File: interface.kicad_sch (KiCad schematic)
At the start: 25 parts, among them J1 QTH-060-03-L-D-A, J2 WE_68715014522_ONE-SIDE, J3 WE_68715014022

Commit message: [#60956] WiP Update symbols references
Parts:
- C1, C2, C3, C4: footprint antmicro-jetson-agx-csi-adapter-footprints:0603-cap -> antmicro-footprints:C_0603_1608Metric; symbol antmicro-jetson-agx-csi-adapter:C_1u_0603 -> antmicroCapacitors0603:C_1u_0603; Author (none) -> Antmicro; License (none) -> Apache-2.0; Manufacturer WALSIN -> KYOCERA AVX; Public (none) -> False
- D1, D2, D3, D4: value LTST-C190GKT -> LED_G_0603_LTST-C190GKT; footprint antmicro-jetson-agx-csi-adapter-footprints:LED_0603 -> antmicro-footprints:LED_0603_1608Metric_G; symbol antmicro-jetson-agx-csi-adapter:LTST-C190GKT -> antmicroLEDIndicationDiscrete:LED_G_0603_LTST-C190GKT; Author (none) -> Antmicro; Color (none) -> Green; License (none) -> Apache-2.0; Manufacturer Lite-On Inc. -> Lite-On; Public (none) -> False
- F1, F2, F3, F4: footprint antmicro-jetson-agx-csi-adapter-footprints:0603-Fuse-Littelfuse-0467 -> antmicro-footprints:F_0603_1608Metric; symbol antmicro-jetson-agx-csi-adapter:04671.25NR -> antmicroFuses:F_1.25A_0603
- J1: value QTH-060-03-L-D-A -> Plug_Samtec_QTH_2x60_QTH-060-03-L-D-A; footprint antmicro-jetson-agx-csi-adapter-footprints:SAMTEC_QTH-060-03-X-D-A -> antmicro-footprints:Conn_Plug_Samtec_QTH_2x60_QTH-060-03-L-D-A; symbol antmicro-jetson-agx-csi-adapter:QTH-060-03-L-D-A -> antmicroB2BConnectors:Plug_Samtec_QTH_2x60_QTH-060-03-L-D-A; Author (none) -> Antmicro; License (none) -> Apache-2.0; Pitch (none) -> 0.5 mm
- R1, R2: footprint antmicro-jetson-agx-csi-adapter-footprints:0805-res -> antmicro-footprints:R_0805_2012Metric; symbol antmicro-jetson-agx-csi-adapter:R_0R_0805 -> antmicroResistorsmisc:R_0R_0805; Author (none) -> Antmicro; Current (none) -> 2.5A; License (none) -> Apache-2.0; Manufacturer VISHAY -> Vishay; Public (none) -> False
- R3, R5: footprint antmicro-jetson-agx-csi-adapter-footprints:0402-res -> antmicro-footprints:R_0402_1005Metric; symbol antmicro-jetson-agx-csi-adapter:R_200R_0402 -> antmicroResistors0402:R_200R_0402
- R4, R6: footprint antmicro-jetson-agx-csi-adapter-footprints:0402-res -> antmicro-footprints:R_0402_1005Metric; symbol antmicro-jetson-agx-csi-adapter:R_470R_0402 -> antmicroResistors0402:R_470R_0402
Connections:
- net GND: now also D1.1 (C), D2.1 (C), D3.1 (C), D4.1 (C), J1.MP; no longer D1.2, D2.2, D3.2, D4.2, J1.G1, J1.G2, J1.G3, J1.G4, J1.G5, J1.G6, J1.G7, J1.G8
- net at R3.2: now also D1.2 (A); no longer D1.1
- net at R4.2: now also D2.2 (A); no longer D2.1
- net at R6.2: now also D4.2 (A); no longer D4.1
- net at R5.2: now also D3.2 (A); no longer D3.1
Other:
- moved on the sheet: C1, C2, C3, C4, R1, R2, TP10, TP11, TP7, TP9

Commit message: [#60956] WiP Update symbols references
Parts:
- removed J2: WE_68715014522_ONE-SIDE, antmicro-jetson-agx-csi-adapter-footprints:WE_68715014522_ONE-SIDE, symbol antmicro-jetson-agx-csi-adapter:WE_68715014522_ONE-SIDE
- removed J3: WE_68715014022, antmicro-jetson-agx-csi-adapter-footprints:WE_68715014022, symbol antmicro-jetson-agx-csi-adapter:WE_68715014022
- added J2: Conn_FFC_WE_68715014522, antmicro-footprints:Conn_FFC_WE_68715014x22, symbol antmicroFCCConnectors:Conn_FFC_WE_68715014522
- added J3: Conn_FFC_WE_68715014022_CUSTOM_FLIPPED, antmicro-footprints:Conn_FFC_WE_68715014x22_CUSTOM_FLIPPED, symbol antmicroFCCConnectors:Conn_FFC_WE_68715014022_CUSTOM_FLIPPED
- F1, F2, F3, F4: value 04671.25NR -> F_1.25A_0603; Author (none) -> Antmicro; License (none) -> Apache-2.0; Manufacturer Littelfuse Inc. -> Littelfuse
- R3, R5: Author (none) -> Antmicro; License (none) -> Apache-2.0; MPN RC0402FR-07200RL -> CR0402-FX-2000GLF; Manufacturer YAGEO -> Bourns; Public (none) -> False; Tolerance (none) -> 1%
- R4, R6: Author (none) -> Antmicro; License (none) -> Apache-2.0; MPN CRCW0402470RFKED -> CR0402-FX-4700GLF; Manufacturer VISHAY -> Bourns; Public (none) -> False; Tolerance (none) -> 1%
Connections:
- net 3V3_FFC_B: now also J2.47, J2.48
- net 3V3_FFC_S: now also J3.47, J3.48
- net 5V_FFC_B: now also J2.49, J2.50
- net 5V_FFC_S: now also J3.49, J3.50
- net CAM0_SCL: now also J2.40
- net CAM0_SDA: now also J2.39
- net CAM1_RST_3V3: now also J3.33
- net CAM1_SCL: now also J2.42
- net CAM1_SDA: now also J2.41
- net CAM2_SCL: now also J3.42
- net CAM2_SDA: now also J3.41
- net CAM3_SCL: now also J3.40
- net CAM3_SDA: now also J3.39
- net CAM_RST_3V3: now also J2.33
- net CSI0_CLK_N: now also J3.28
- net CSI0_CLK_P: now also J3.29
- net CSI0_D0_N: now also J3.25
- net CSI0_D0_P: now also J3.26
- net CSI0_D1_N: now also J3.23
- net CSI0_D1_P: now also J3.24
- net CSI1_D0_N: now also J3.21
- net CSI1_D0_P: now also J3.22
- net CSI1_D1_N: now also J3.19
- net CSI1_D1_P: now also J3.20
- net CSI2_CLK_N: now also J3.10
- net CSI2_CLK_P: now also J3.11
- net CSI2_D0_N: now also J3.7
- net CSI2_D0_P: now also J3.8
- net CSI2_D1_N: now also J3.5
- net CSI2_D1_P: now also J3.6
- net CSI3_D0_N: now also J3.3
- net CSI3_D0_P: now also J3.4
- net CSI3_D1_N: now also J3.1
- net CSI3_D1_P: now also J3.2
- net CSI4_CLK_N: now also J2.29
- net CSI4_CLK_P: now also J2.28
- net CSI4_D0_N: now also J2.25
- net CSI4_D0_P: now also J2.26
- net CSI4_D1_N: now also J2.23
- net CSI4_D1_P: now also J2.24
- net CSI5_D1_N: now also J2.19
- net CSI5_D1_P: now also J2.20
- net CSI6_CLK_N: now also J2.10
- net CSI6_CLK_P: now also J2.11
- net CSI6_D0_N: now also J2.7
- net CSI6_D0_P: now also J2.8
- net CSI6_D1_N: now also J2.5
- net CSI6_D1_P: now also J2.6
- net CSI7_D0_N: now also J2.3
- net CSI7_D0_P: now also J2.4
- net CSI7_D1_N: now also J2.1
- net CSI7_D1_P: now also J2.2
- net GND: now also J2.12, J2.15, J2.18, J2.27, J2.30, J2.9, J2.MP1 (MP), J2.MP2 (MP), J3.12, J3.15, J3.18, J3.27, J3.30, J3.9, J3.MP1 (MP), J3.MP2 (MP)
- net VSYNC_CAM0_3V3: now also J2.32
- net VSYNC_CAM1_3V3: now also J2.34
- net VSYNC_CAM2_3V3: now also J3.34
- net VSYNC_CAM3_3V3: now also J3.32
- net CSI1_CLK_N: no longer names the net of J1.10
- net CSI1_CLK_P: no longer names the net of J1.8
- net CSI3_CLK_N: no longer names the net of J1.28
- net CSI3_CLK_P: no longer names the net of J1.26
- net CSI5_CLK_N: no longer names the net of J1.67
- net CSI5_CLK_P: no longer names the net of J1.65
- net CSI5_D0_N: no longer names the net of J1.61
- net CSI5_D0_P: no longer names the net of J1.59
- net CSI7_CLK_N: no longer names the net of J1.68
- net CSI7_CLK_P: no longer names the net of J1.66
- no-connect marks 60 -> 72
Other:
- note added: "CSI1_CLK_N"
- note added: "CSI1_CLK_P"
- note added: "CSI3_CLK_N"
- note added: "CSI3_CLK_P"
- note added: "CSI5_CLK_N"
- note added: "CSI5_CLK_P"
- note added: "CSI5_D0_N"
- note added: "CSI5_D0_P"
- note added: "CSI7_CLK_N"
- note added: "CSI7_CLK_P"
- moved on the sheet: C3, C4, D3, D4, J1, R1, R2, TP10, TP11, TP7, TP9

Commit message: [#60956] WiP Update footprints
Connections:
- net CSI1_CLK_N: now reaches J1.10
- net CSI3_CLK_P: now reaches J1.26
- net CSI3_CLK_N: now reaches J1.28
- net CSI5_D0_P: now reaches J1.59
- net CSI5_D0_P: now also J2.22
- net CSI5_D0_N: now reaches J1.61
- net CSI5_D0_N: now also J2.21
- net CSI5_CLK_P: now reaches J1.65
- net CSI7_CLK_P: now reaches J1.66
- net CSI5_CLK_N: now reaches J1.67
- net CSI7_CLK_N: now reaches J1.68
- net CSI1_CLK_P: now reaches J1.8
- no-connect marks 72 -> 60
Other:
- note removed: "CSI1_CLK_N"
- note removed: "CSI1_CLK_P"
- note removed: "CSI3_CLK_N"
- note removed: "CSI3_CLK_P"
- note removed: "CSI5_CLK_N"
- note removed: "CSI5_CLK_P"
- note removed: "CSI5_D0_N"
- note removed: "CSI5_D0_P"
- note removed: "CSI7_CLK_N"
- note removed: "CSI7_CLK_P"

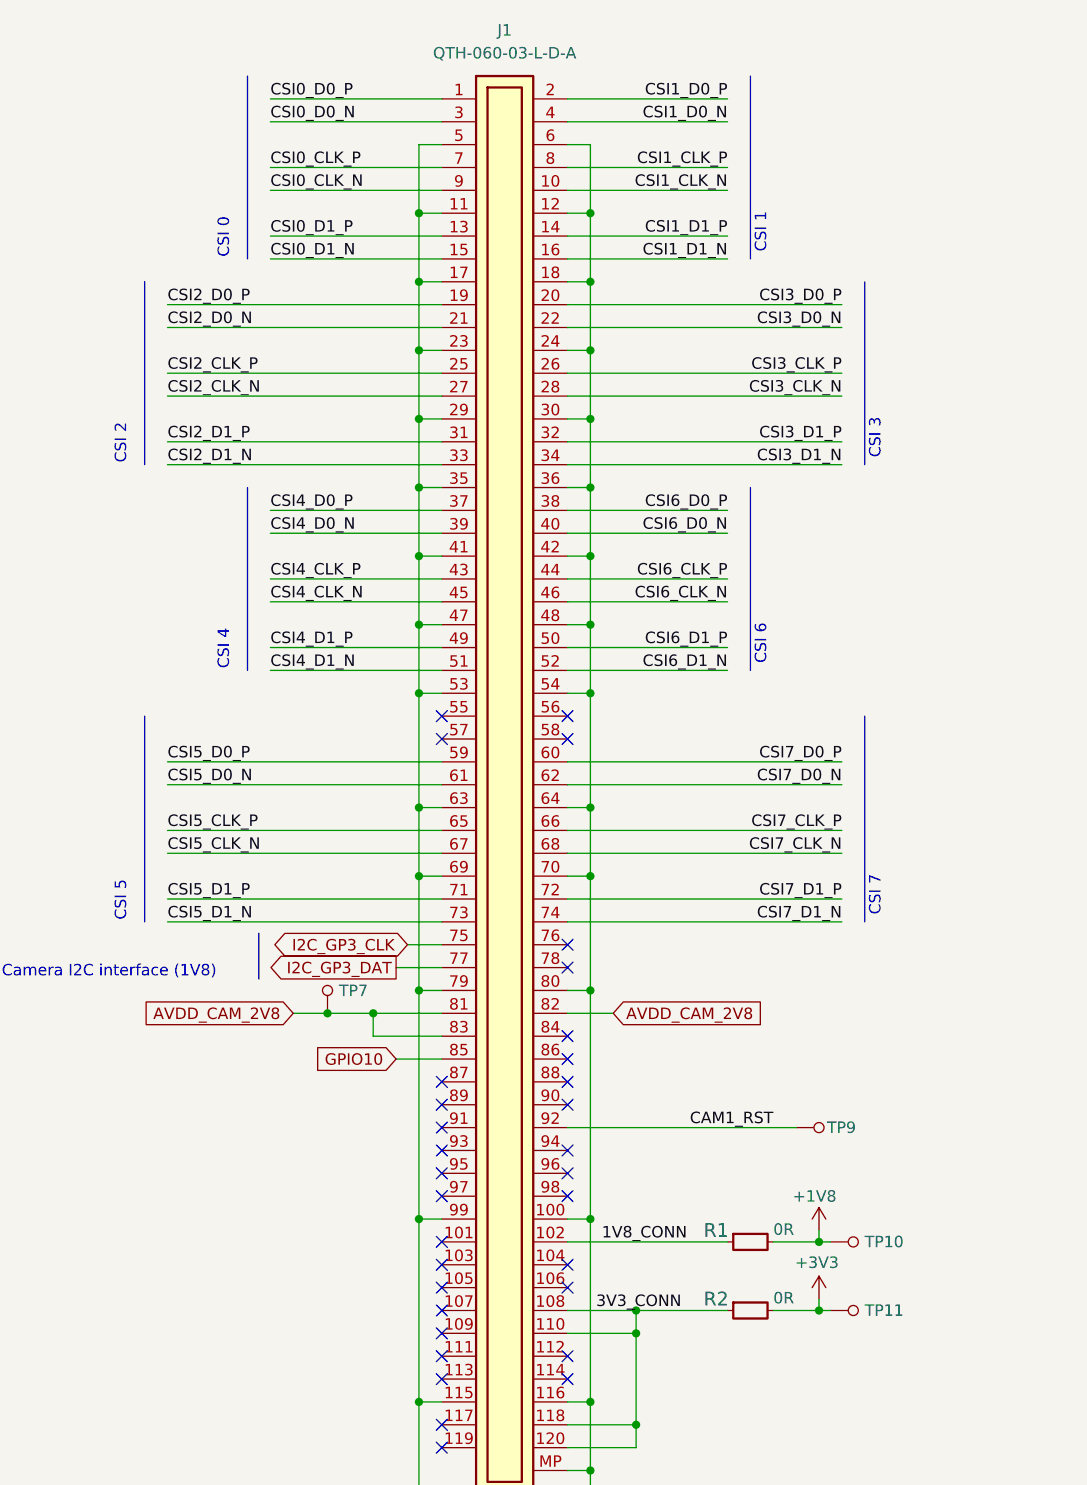
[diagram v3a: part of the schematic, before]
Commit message: [#60956] Update B340A-13-F,MAX1708EEE+ and TP_0_75mm from library
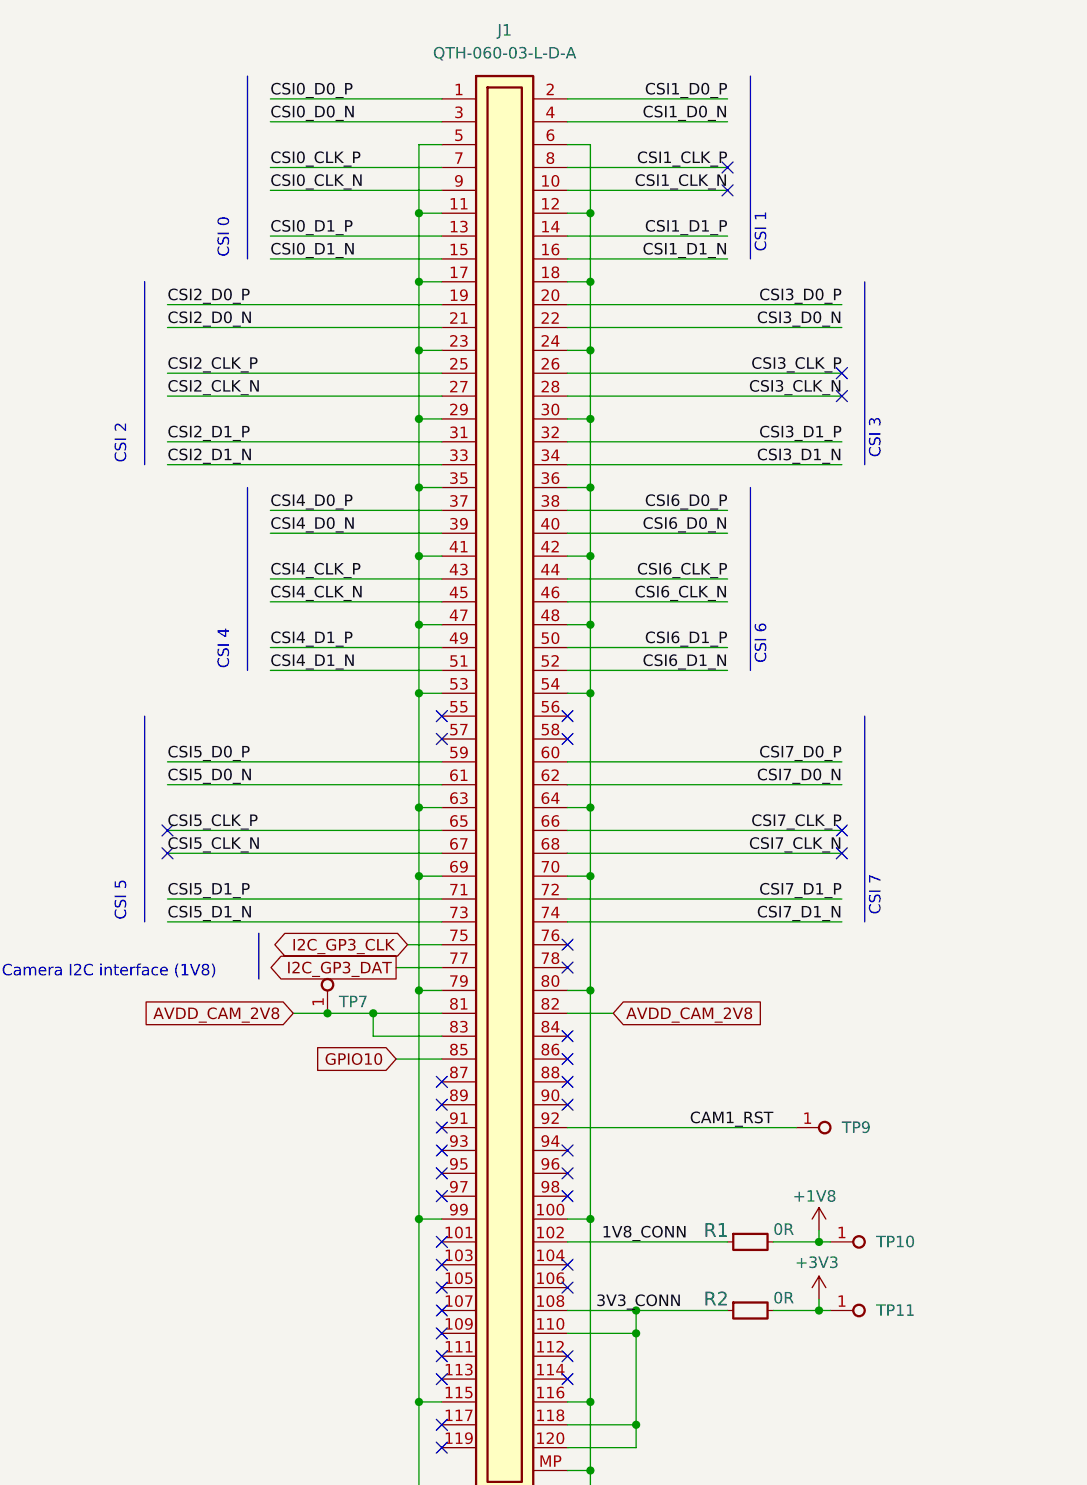
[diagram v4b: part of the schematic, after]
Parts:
- removed TP10, TP11, TP7, TP9: TP_SMD_0_75MM, antmicro-jetson-agx-csi-adapter-footprints:Testpoint_smd_0_75mm, symbol antmicro-jetson-agx-csi-adapter:TP_SMD_0_75MM
- added TP10, TP11, TP7, TP9: TP_0.75mm_SMD, antmicro-footprints:TP_SMD_0.75mm, symbol antmicroTestPoints:TP_0.75mm_SMD
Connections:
- net +1V8: now also TP10.1
- net +3V3: now also TP11.1
- net AVDD_CAM_2V8: now also TP7.1
- net CAM1_RST: now also TP9.1
- no-connect marks 60 -> 68
